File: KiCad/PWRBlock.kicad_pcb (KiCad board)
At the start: 2 copper layers, 58 parts, among them IC1 MINI360, IC2 ATMEGA8-AI, P1 CONN_02X02, P2 BatIn, P4 CONN_02X04, P5 ESD, Q1 Q_NMOS_GSD, Q2 Q_NMOS_GSD, Q3 Q_NMOS_GSD, Q4 Q_NMOS_GSD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

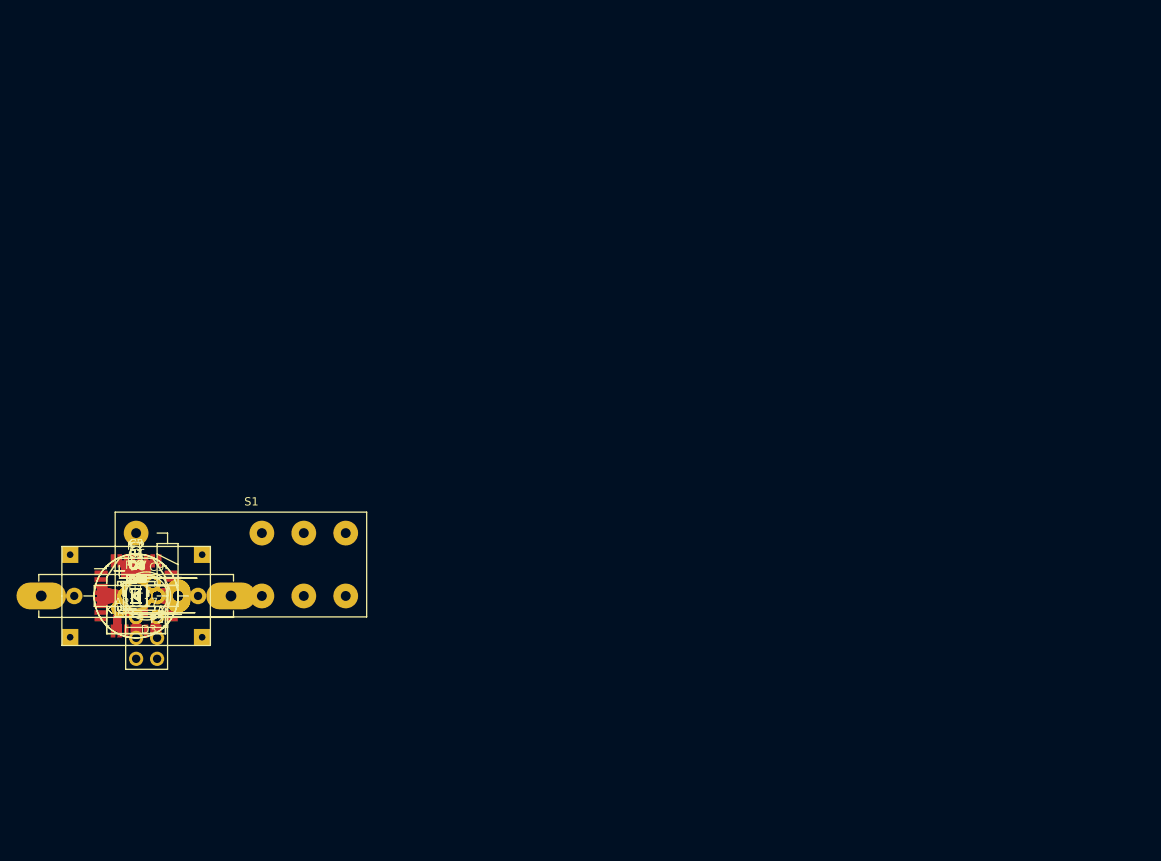
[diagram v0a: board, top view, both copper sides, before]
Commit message: Platienengröße geändert
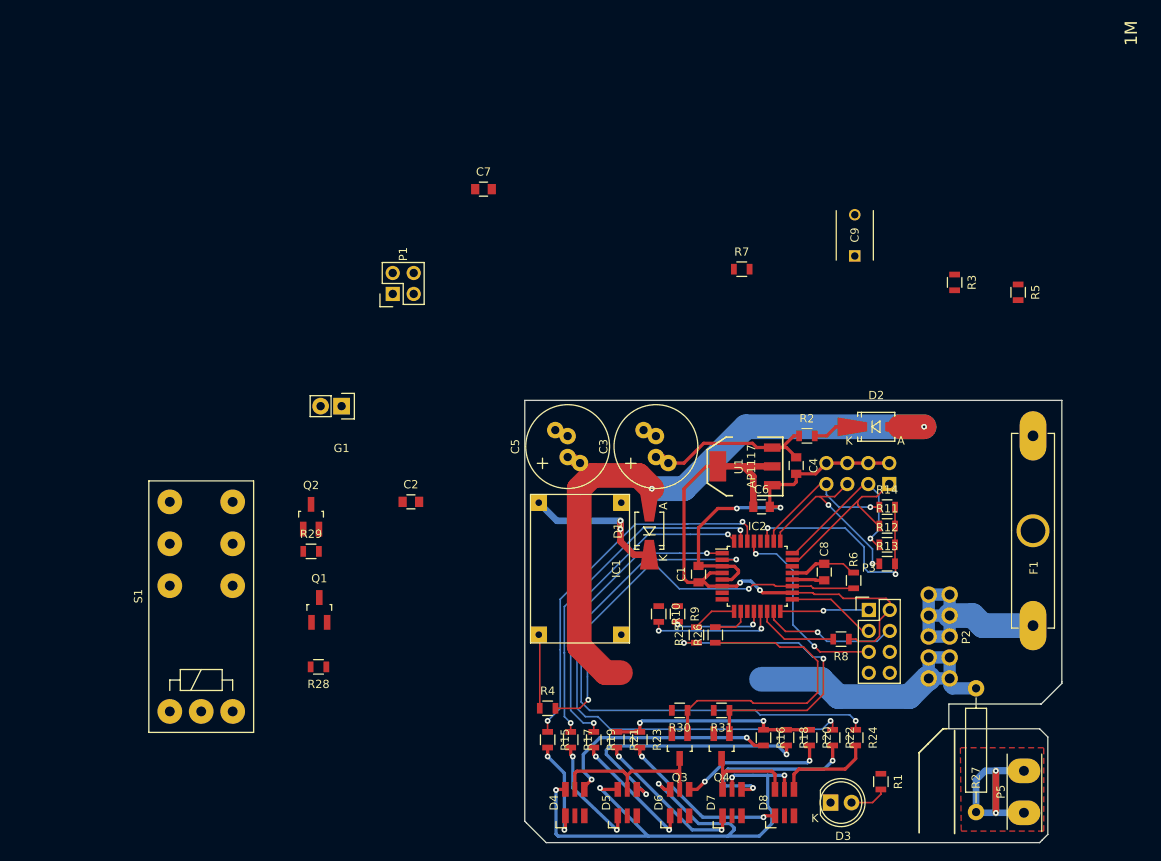
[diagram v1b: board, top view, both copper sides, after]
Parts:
- added P3: CONN_02X04, Pin_Headers:Pin_Header_Straight_2x04, F.Cu at (237.3, 106.7)
- added R28: 1k, Resistors_SMD:R_0805, F.Cu at (170.6, 113.6)
- added R29: 1k, Resistors_SMD:R_0805, F.Cu at (169.7, 99.6)
- added R30: 1k, Resistors_SMD:R_0805, F.Cu at (214.4, 118.9)
- added R31: 1k, Resistors_SMD:R_0805, F.Cu at (219.5, 118.9)
- D4, D5, D6, D7, D8: footprint Sven:SMD_LED_4Pin_special -> LEDs2:LRTB_G6TG
- P4: moved to B.Cu
- moved R5 113.1 mm to (255.4, 68.2), turned to 270 degrees
- moved P5 109.7 mm to (256.1, 126.2), turned to 270 degrees
- moved F1 109.0 mm to (257.2, 97.1), turned to 90 degrees
- moved R3 106.2 mm to (247.7, 67.0), turned to 270 degrees
- moved R27 103.5 mm to (250.3, 123.7), turned to 270 degrees
- moved P2 99.1 mm to (247.1, 115.0), turned to 90 degrees
- moved C9 96.4 mm to (235.6, 63.8), turned to 90 degrees
- moved R1 93.0 mm to (238.8, 127.5), turned to 270 degrees
- moved P4 92.3 mm to (239.8, 91.4), turned to 90 degrees
- moved D2 92.0 mm to (238.2, 84.5)
- moved R14 91.7 mm to (239.5, 94.2)
- moved R11 91.4 mm to (239.5, 96.5)
- moved R12 91.2 mm to (239.5, 98.8)
- moved R13 91.1 mm to (239.5, 101.1)
- moved R24 88.9 mm to (235.7, 122.2), turned to 270 degrees
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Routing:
- net GND: track 0.00 -> 156.4 mm, vias 0 -> 7
- net VCC: track 0.00 -> 92.3 mm, vias 0 -> 2
- net +5VA: track 0.00 -> 71.3 mm, vias 0 -> 2
- net Net-(IC2-Pad2): track 0.00 -> 68.5 mm, vias 0 -> 2
- net Net-(IC2-Pad1): track 0.00 -> 65.4 mm, vias 0 -> 2
- net /Sens5V: track 0.00 -> 50.1 mm, vias 0 -> 2
- net Net-(IC2-Pad30): track 0.00 -> 45.3 mm, vias 0 -> 2
- net Net-(IC2-Pad31): track 0.00 -> 42.2 mm, vias 0 -> 2
- net Net-(IC2-Pad32): track 0.00 -> 40.5 mm, vias 0 -> 2
- net /AllRed: track 0.00 -> 38.6 mm, vias 0 -> 2
- net /AllBlue: track 0.00 -> 37.1 mm
- net +5V: track 0.00 -> 34.6 mm, vias 0 -> 2
- net Net-(D5-Pad4): track 0.00 -> 32.3 mm, vias 0 -> 2
- net /ESD: track 0.00 -> 30.0 mm, vias 0 -> 2
- net Net-(IC2-Pad27): track 0.00 -> 29.1 mm, vias 0 -> 2
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- added copper zone on F.Cu, net /ESD
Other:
- board outline added: 65.1 x 53.6 mm
- net class 12V added: clearance 0.4, trace_width 0.2, via_dia 0.7, via_drill 0.3
- net class Default: trace_width 0.25 -> 0.2; via_dia 0.6 -> 0.7; via_drill 0.4 -> 0.3
- board text added: "1M"
